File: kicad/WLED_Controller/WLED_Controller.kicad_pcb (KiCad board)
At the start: 2 copper layers, 72 x 50 mm, 45 parts, among them J1 USB_C_Receptacle_USB2.0, J2 Conn_01x03, J3 Conn_01x03, J4 Conn_01x03, J6 Conn_01x02, Q1 BC847, Q2 BC847, SW1 SW_RESET, SW2 SW_BOOT, SW3 SW_Push, U1 ESP32-WROOM-32, U2 CH340C, U3 NCP1117-3.3, U4 TSSP58P38, U5 74HC14

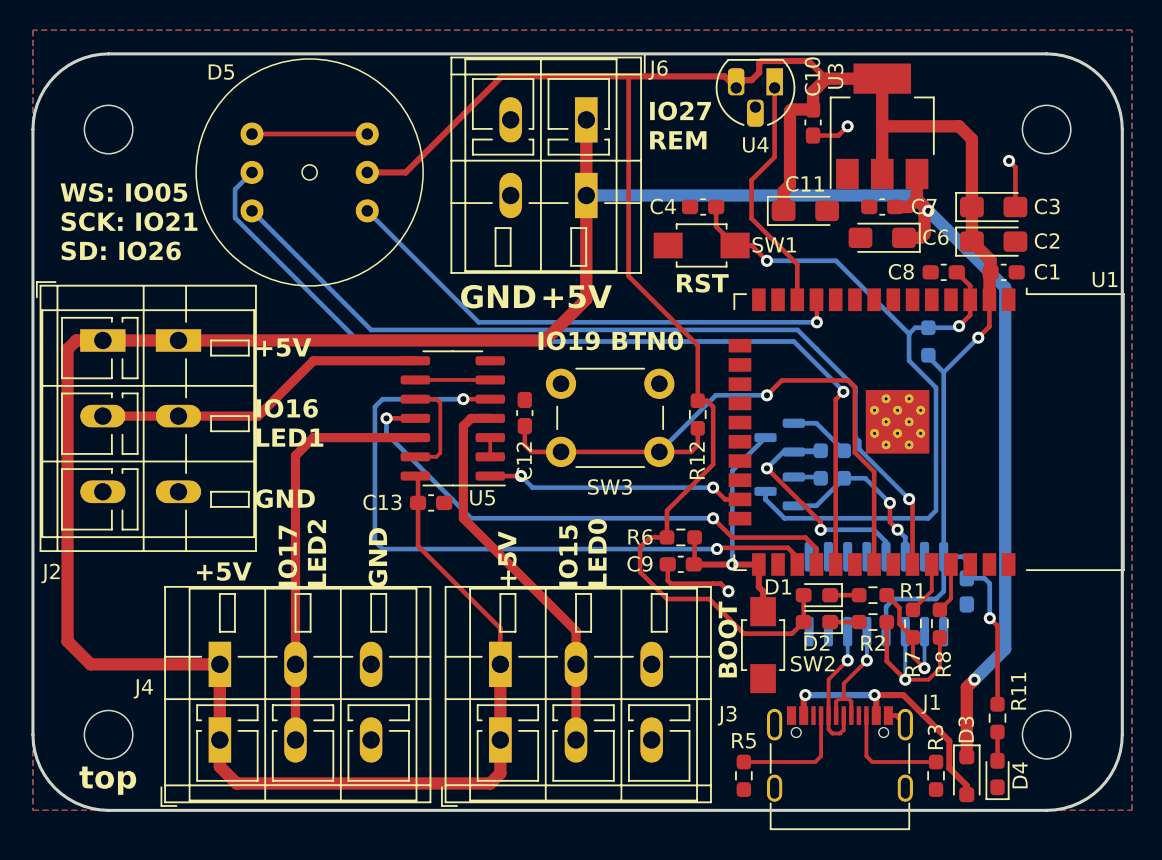
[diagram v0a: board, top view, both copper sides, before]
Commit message: Change to WAGO250
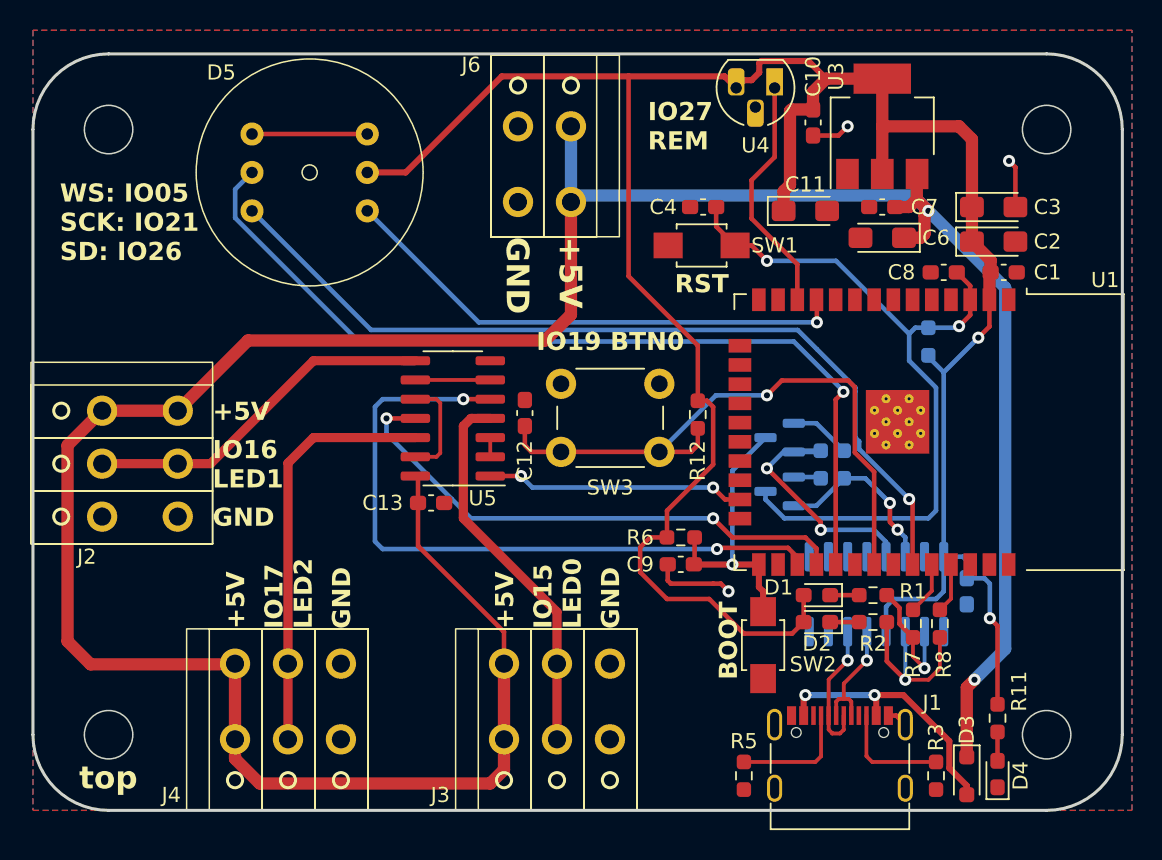
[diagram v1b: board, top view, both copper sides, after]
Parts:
- J2, J3, J4: footprint GioN_Custom:TerminalBlock_WAGO_236-403_1x03_P5.00mm_45Degree -> GioN_Custom:WAGO_250-203_1x03_P3.50mm
- J6: footprint GioN_Custom:TerminalBlock_WAGO_236-402_1x02_P5.00mm_45Degree -> GioN_Custom:WAGO_250-202_1x02_P3.50mm
- moved J2 13.6 mm to (11.9, -17.6)
- moved J4 10.1 mm to (22.2, -12.0)
- moved J3 9.34 mm to (39.9, -12.0)
- moved J6 6.88 mm to (30.3, -37.9)
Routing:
- net +5V: track 195.3 -> 190.9 mm
- net Net-(J2-Pin_2): track 22.2 -> 23.5 mm
- net Net-(J3-Pin_2): track 25.8 -> 25.3 mm
